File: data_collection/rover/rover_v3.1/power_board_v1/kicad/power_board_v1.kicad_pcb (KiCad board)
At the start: 4 copper layers, 90 x 65 mm, 131 parts, among them J1 XT60_BATT, J10 from Pi USB2, J11 UPDI prog (UPDI/3V3/GND), J12 XT30 fallback pads, J2 PANEL_SW, J3 USB4105-GF-A (TH shell), J4 USB_A radio1, J5 USB_A radio2, J6 AUX 5V 2A, J7 PI GPIO harness, J8 AUX_CTL out (JST-GH), J9 from Pi USB1, Q2 CSD18543Q3A diode, Q3 CSD18543Q3A switch, U1 LM5145 rail A, U2 LM5145 rail B, U3 ATtiny816 (VQFN), U4 LM74800-Q1, U5 INA226 (addr 0x40), U6 TPS7A1633 3V3 60V LDO, U7 TPS2553 1.7A, U8 TPS2553 1.7A, U9 AP2112K-3.3 (switched)

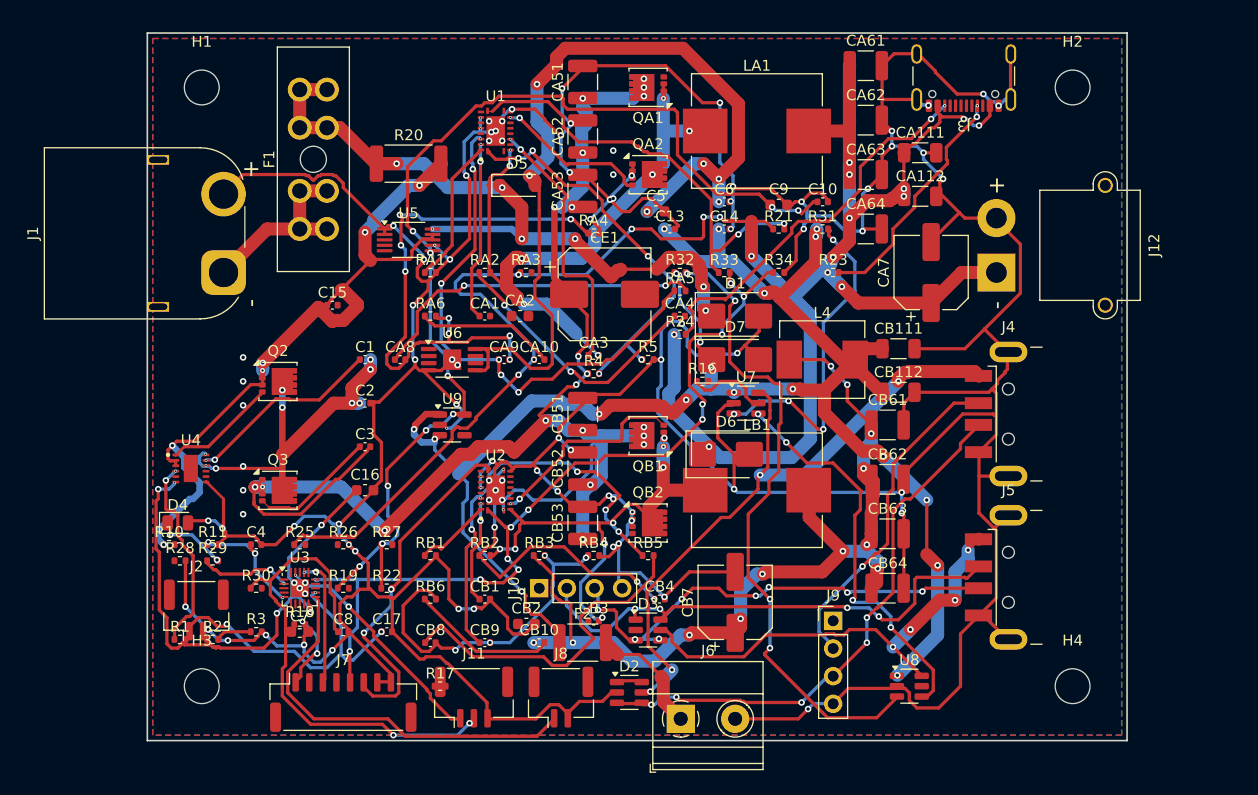
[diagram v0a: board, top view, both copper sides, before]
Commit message: WIP: 3-port board regen — schematic final+verified (133 comps, TPS2557 x3); PLACEMENT NOT CONVERGED (24 overlaps: right edge cannot fit J13+J12+J4+J5; J12 top-edge spot collides LA1) — needs placement iteration before routing/DeepPCB resubmit. DO NOT start stale DeepPCB jobs (pre-3-port netlist). Audit gates correctly failing on this WIP
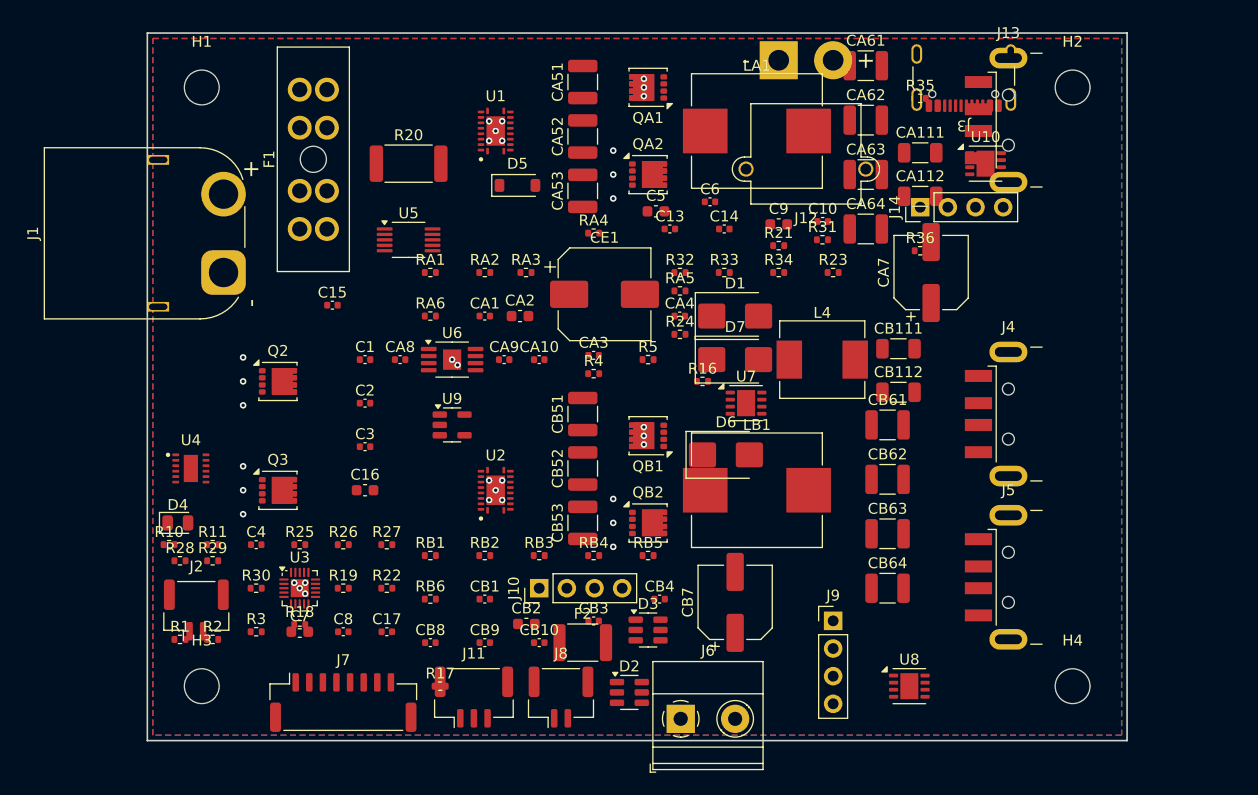
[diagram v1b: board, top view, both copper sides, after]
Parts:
- added J13: USB_A port3 (3A), USB_A_CNCTech_1001-011-01101_Horizontal, F.Cu at (136.0, 58.0)
- added J14: from Pi USB3, PinHeader_1x04_P2.54mm_Vertical, F.Cu at (121.0, 66.0)
- added R35: 100k EN3 pu, R_0402_1005Metric, F.Cu at (121.0, 56.0)
- added R36: 20k RILIM3 (~3A), R_0402_1005Metric, F.Cu at (121.0, 70.0)
- added U10: TPS2557 ~3A (always on), VSON-8-1EP_3x3mm_P0.65mm_EP1.65x2.4mm, F.Cu at (127.0, 62.0)
- CB4: value 22p CILIM -> 18p CILIM
- R16: value 20k RILIM1 (1.2A) -> 20k RILIM1 (~3A)
- R17: value 20k RILIM2 (1.2A) -> 20k RILIM2 (~3A)
- RB2: value 261R RILIM (wc-min 4.8A) -> 348R RILIM (wc-min 6.3A)
- U7, U8: value TPS2553 1.7A -> TPS2557 ~3A; footprint SOT-23-6 -> VSON-8-1EP_3x3mm_P0.65mm_EP1.65x2.4mm
- moved J12 27.9 mm to (108.0, 52.5), turned to 180 degrees
- moved C10 1.81 mm to (112.0, 67.3)
- moved C9 1.80 mm to (108.0, 67.6)
- moved R21 1.53 mm to (108.0, 69.5)
- moved C6 1.31 mm to (101.7, 65.5)
- moved R31 0.99 mm to (112.0, 69.0)
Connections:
- U7 pad 1: 5V_B -> GND
- U7 pad 2: GND -> 5V_B
- U7 pad 3: EN_USB1 -> 5V_B
- U7 pad 4: FAULT_USB -> EN_USB1
- U8 pad 1: 5V_B -> GND
- U8 pad 2: GND -> 5V_B
- U8 pad 3: EN_USB2 -> 5V_B
- U8 pad 4: FAULT_USB -> EN_USB2
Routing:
- net GND: track 617.2 -> 0.00 mm, vias 96 -> 28
- net 5V_A: track 192.3 -> 0.00 mm, vias 19 -> 0
- net 5V_B: track 159.5 -> 0.00 mm, vias 19 -> 0
- net VSW: track 132.1 -> 0.00 mm, vias 21 -> 6
- net 3V3_SW: track 101.5 -> 0.00 mm, vias 10 -> 0
- net VBATT_FD: track 83.5 -> 0.00 mm, vias 6 -> 0
- net 5VB_PRE: track 82.1 -> 0.00 mm, vias 12 -> 0
- net PGOOD_A: track 80.0 -> 0.00 mm, vias 12 -> 0
- net VBATT_S: track 67.5 -> 0.00 mm, vias 6 -> 0
- net VBATT_F: track 66.6 -> 0.00 mm, vias 7 -> 0
- net VBUS1: track 60.5 -> 0.00 mm, vias 4 -> 0
- net EN_USB2: track 59.6 -> 0.00 mm, vias 4 -> 0
- net SW_A: track 59.5 -> 0.00 mm, vias 8 -> 0
- net FB_A: track 51.7 -> 0.00 mm, vias 8 -> 0
- net D1_P: track 50.9 -> 0.00 mm, vias 5 -> 0
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
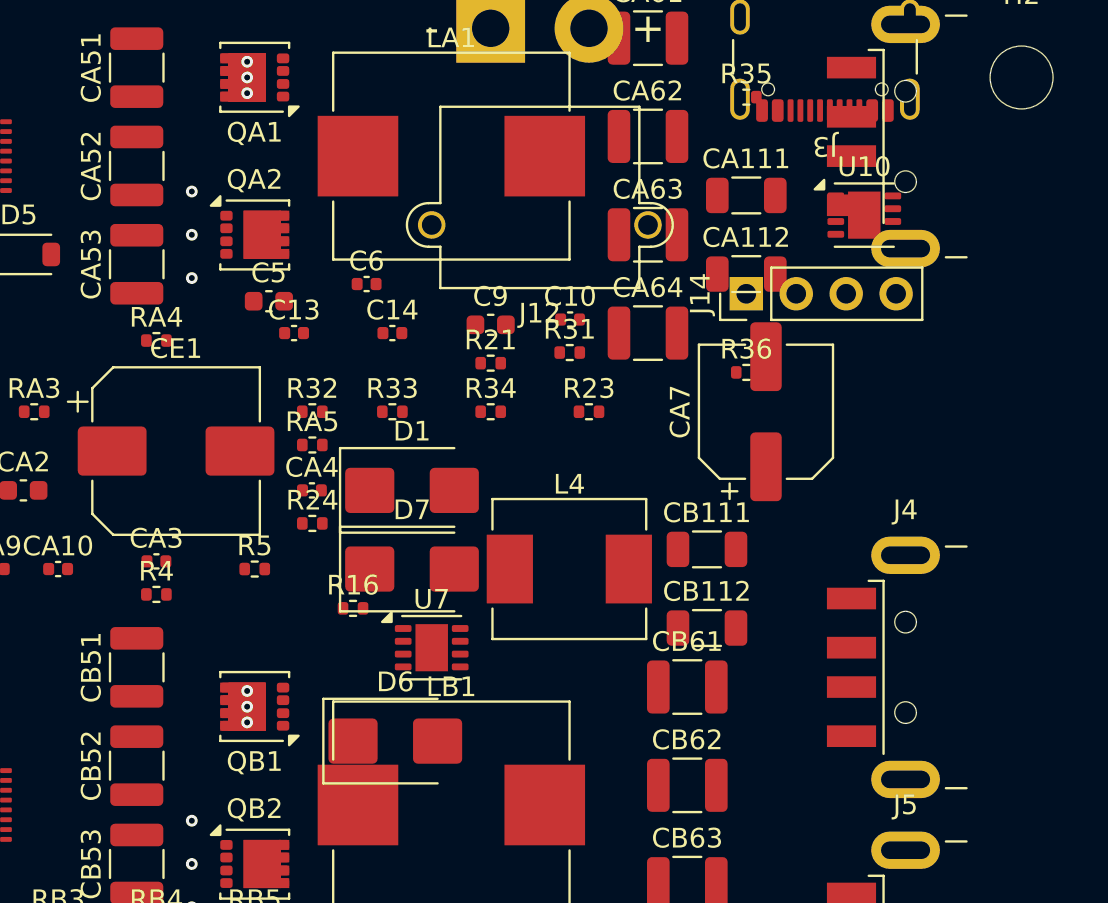
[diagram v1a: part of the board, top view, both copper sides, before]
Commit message: WIP 3-port placement iteration 2: XT30 -> inboard pigtail header pads; port-3 cluster movable grid V; 24->20 overlaps. GEOMETRIC CONSTRAINT FOUND: board edges cannot host a 3rd horizontal USB-A (J13's 23mm span collides with J3-top / LA1 / J1-left / J7-J6-bottom on every edge) — needs user decision: vertical USB-A mid-board, panel-mount pigtail header, or +10mm board width
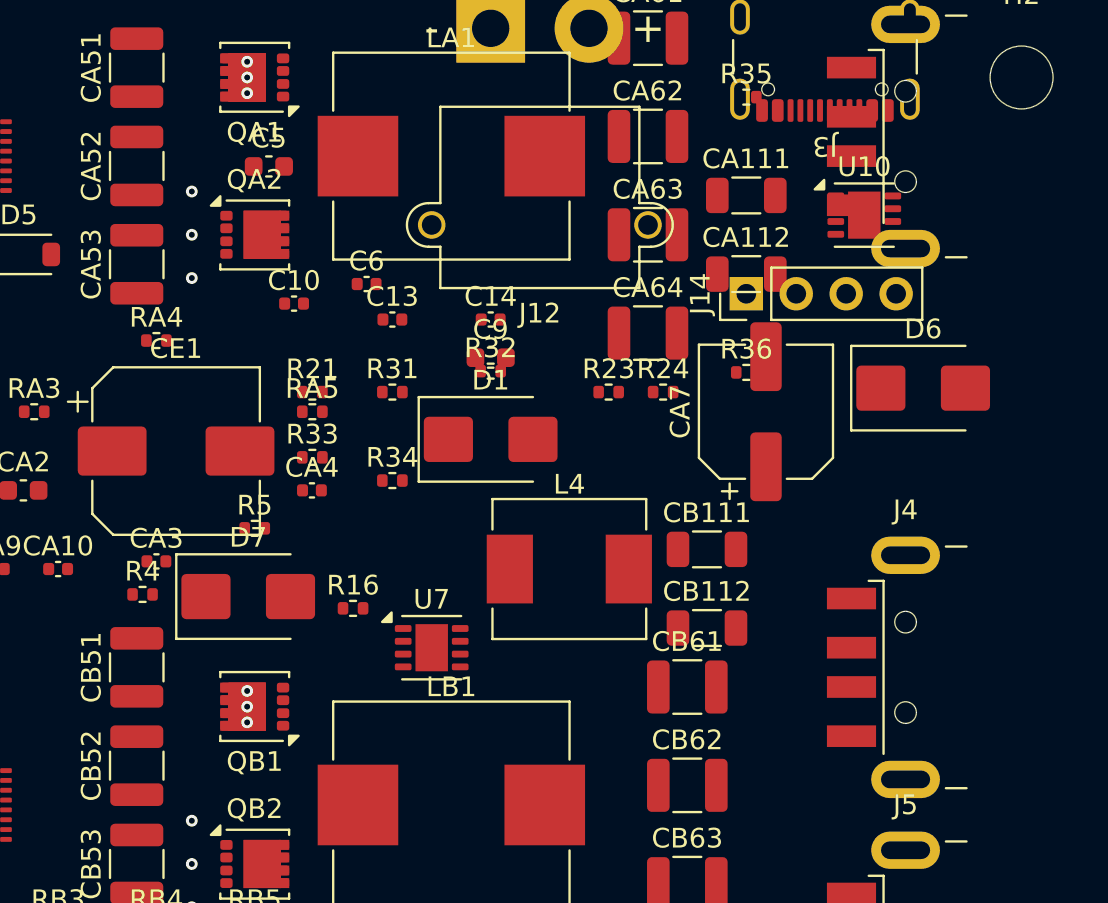
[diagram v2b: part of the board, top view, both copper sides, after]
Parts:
- moved D6 32.3 mm to (130.0, 70.8)
- moved R24 19.0 mm to (116.8, 71.0)
- moved C10 14.1 mm to (98.0, 66.5)
- moved R32 9.30 mm to (108.0, 69.9)
- moved R31 9.24 mm to (103.0, 71.0)
- moved R21 9.19 mm to (98.9, 71.0)
- moved D7 8.45 mm to (95.7, 81.4)
- moved C5 6.85 mm to (96.7, 59.5)
- moved R34 6.10 mm to (103.0, 75.5)
- moved C13 5.05 mm to (103.0, 67.3)
- moved C14 5.05 mm to (108.0, 67.3)
- moved D1 4.77 mm to (108.0, 73.4)
- moved R33 4.68 mm to (98.9, 74.3)
- moved R5 2.07 mm to (96.0, 77.9)
- moved RA5 1.69 mm to (98.9, 72.0)
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
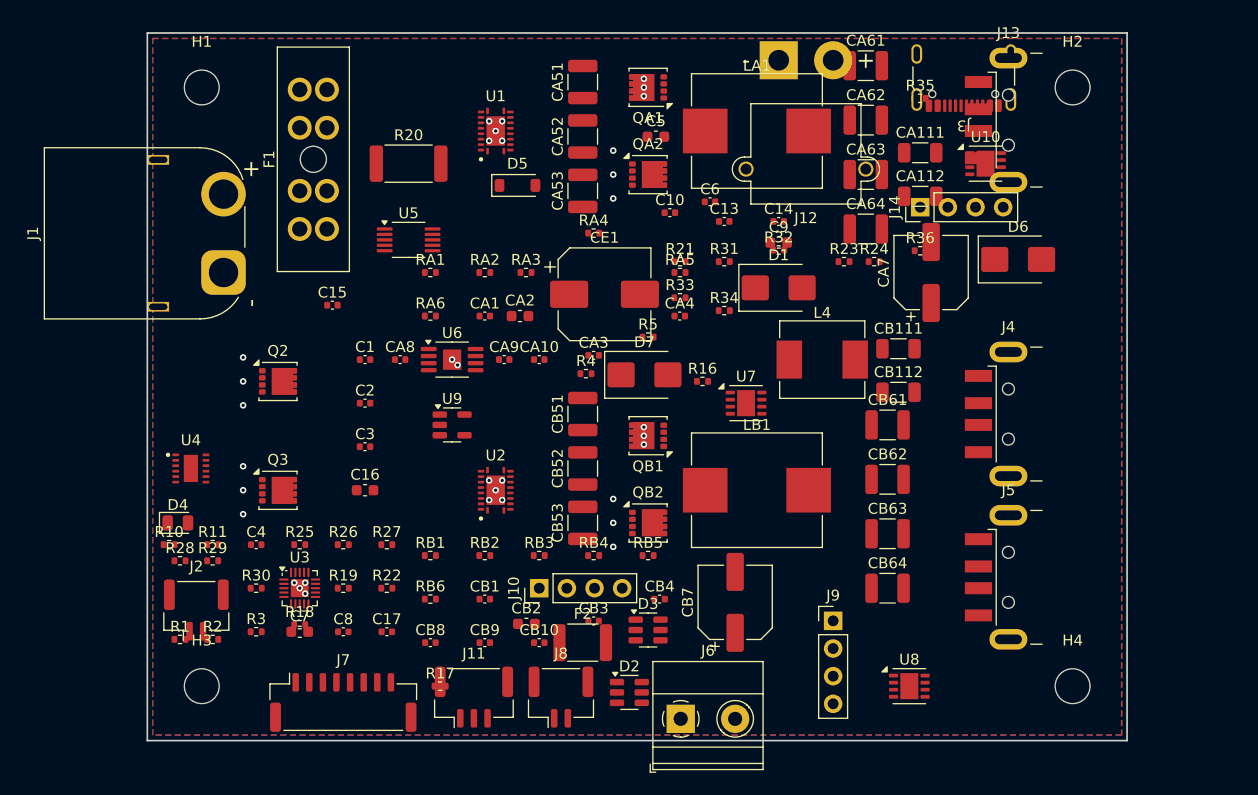
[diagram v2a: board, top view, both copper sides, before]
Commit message: v4 board: 100x65, 3x USB-A on right edge (invariant PASS), KRT-routed (180/211 multipoint + imported: 42 unconnected, 98 clearance to triage); DeepPCB v4 pair submitted (protected + scratch) with net classes
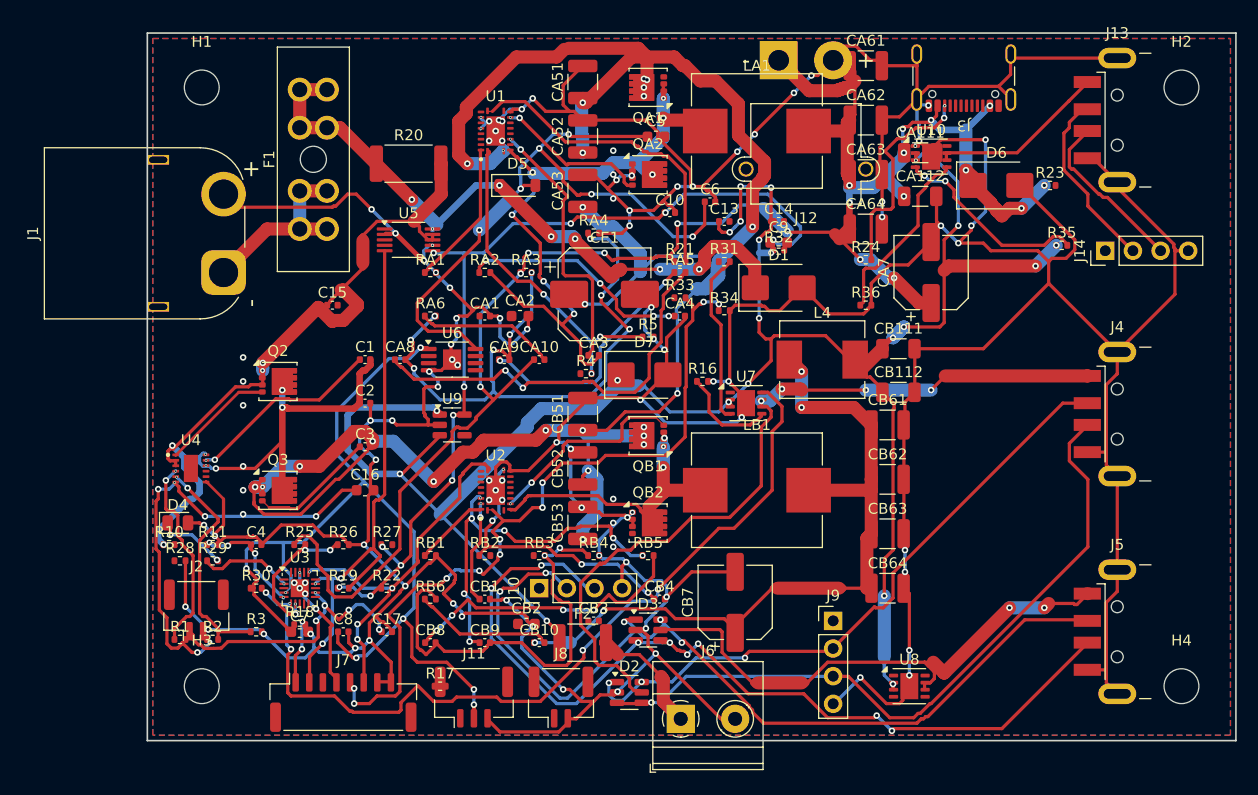
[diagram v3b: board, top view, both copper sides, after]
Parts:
- moved R23 20.2 mm to (132.9, 64.0)
- moved R35 18.7 mm to (134.0, 69.5)
- moved J14 17.5 mm to (138.0, 70.0)
- moved J5 11.2 mm to (146.0, 105.0)
- moved H2 10.0 mm to (145.0, 55.0)
- moved H4 10.0 mm to (145.0, 110.0)
- moved J13 10.0 mm to (146.0, 58.0)
- moved J4 10.0 mm to (146.0, 85.0)
- moved D6 7.09 mm to (128.0, 64.0)
- moved R36 7.07 mm to (116.0, 75.0)
- moved U10 5.04 mm to (122.0, 61.4)
- moved R24 0.79 mm to (116.0, 70.8)
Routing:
- net GND: track 0.00 -> 659.7 mm, vias 28 -> 105
- net 5V_B: track 0.00 -> 197.8 mm, vias 0 -> 21
- net VSW: track 0.00 -> 195.5 mm, vias 6 -> 24
- net 5V_A: track 0.00 -> 166.1 mm, vias 0 -> 18
- net MCU_3V3: track 0.00 -> 84.8 mm, vias 0 -> 7
- net D2_P: track 0.00 -> 84.4 mm, vias 0 -> 8
- net 3V3_SW: track 0.00 -> 84.2 mm, vias 0 -> 11
- net D2_N: track 0.00 -> 82.7 mm, vias 0 -> 5
- net FAULT_USB: track 0.00 -> 79.0 mm, vias 0 -> 5
- net VBUS1: track 0.00 -> 74.1 mm, vias 0 -> 4
- net PGOOD_A: track 0.00 -> 71.7 mm, vias 0 -> 10
- net 5VB_PRE: track 0.00 -> 68.1 mm, vias 0 -> 4
- net D1_P: track 0.00 -> 65.5 mm, vias 0 -> 1
- net VBATT_S: track 0.00 -> 64.2 mm, vias 0 -> 4
- net VBATT_F: track 0.00 -> 61.6 mm, vias 0 -> 7
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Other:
- board size 90 x 65 mm -> 100 x 65 mm
